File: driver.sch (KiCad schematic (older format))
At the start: 53 parts, among them J1 Screw_Terminal_01x02, J2 Conn_02x16_Odd_Even, Q1 Q_NMOS_GDSD, Q10 Q_NMOS_GDSD, Q11 Q_NMOS_GDSD, Q12 Q_NMOS_GDSD, Q13 Q_NMOS_GDSD, Q14 Q_NMOS_GDSD, Q15 Q_NMOS_GDSD, Q16 Q_NMOS_GDSD, Q17 AOD417 Q_PMOS_DGS, Q2 Q_NMOS_GDSD, Q3 Q_NMOS_GDSD, Q4 Q_NMOS_GDSD, Q5 Q_NMOS_GDSD, Q6 Q_NMOS_GDSD, Q7 Q_NMOS_GDSD, Q8 Q_NMOS_GDSD, Q9 Q_NMOS_GDSD, SW1 SW_Push, U1 PCA9685PW

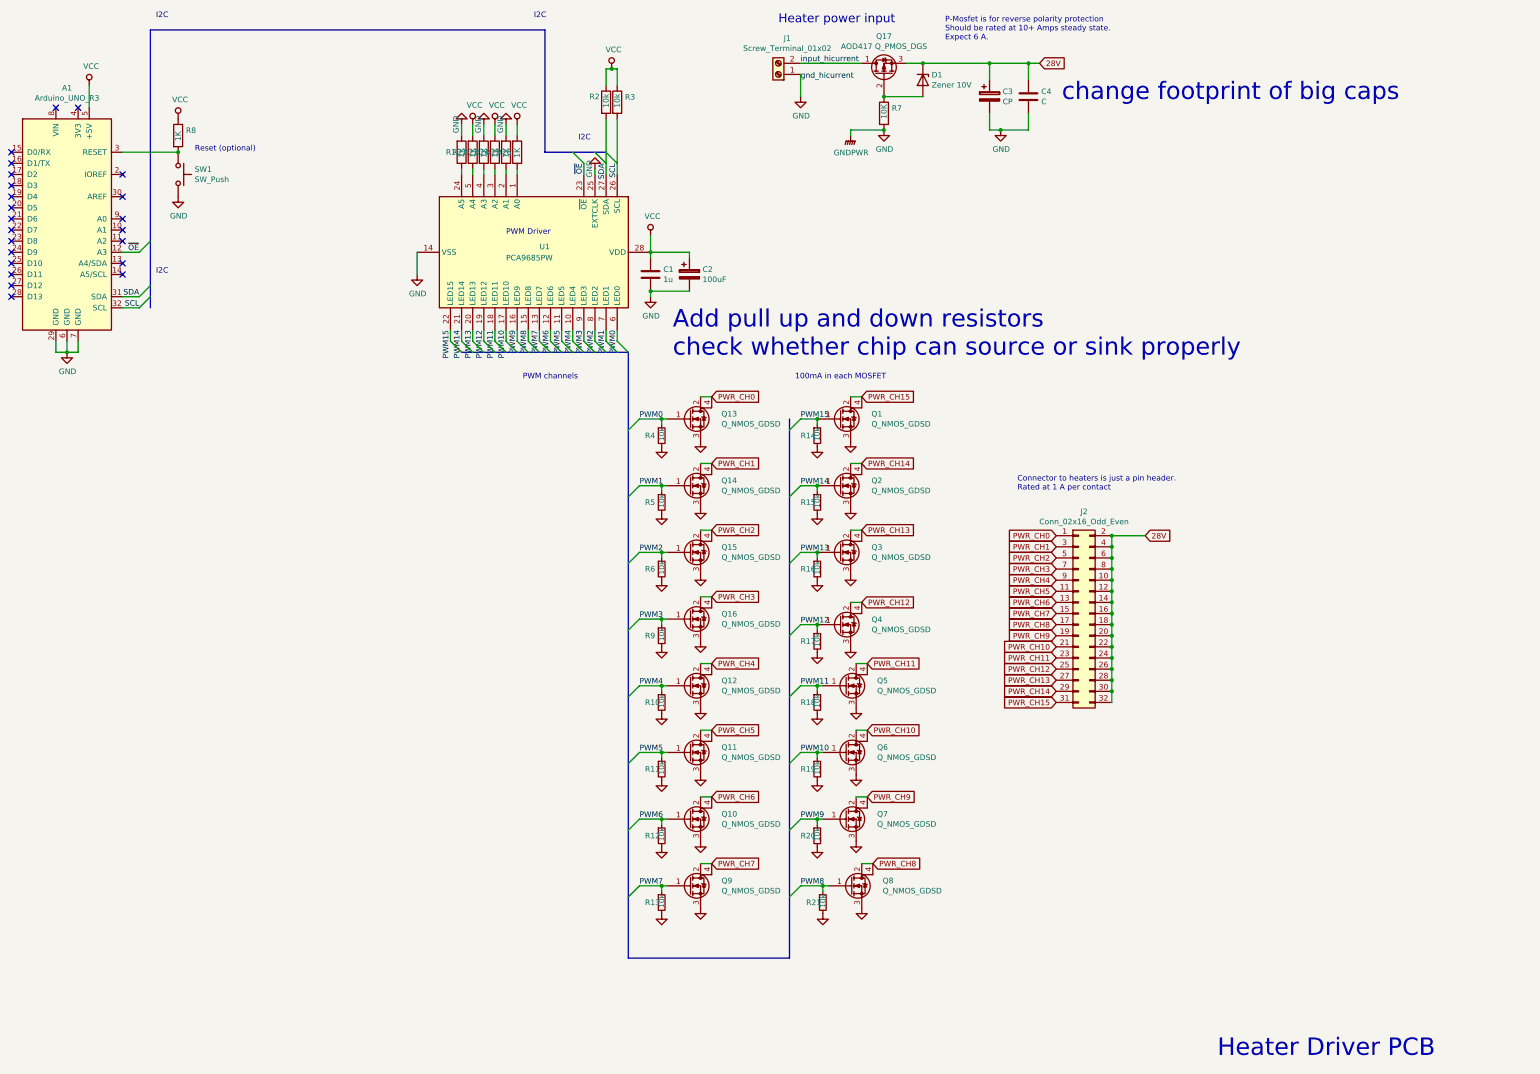
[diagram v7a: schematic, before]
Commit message: Change all resistors to 10K 0805. More routing and placement
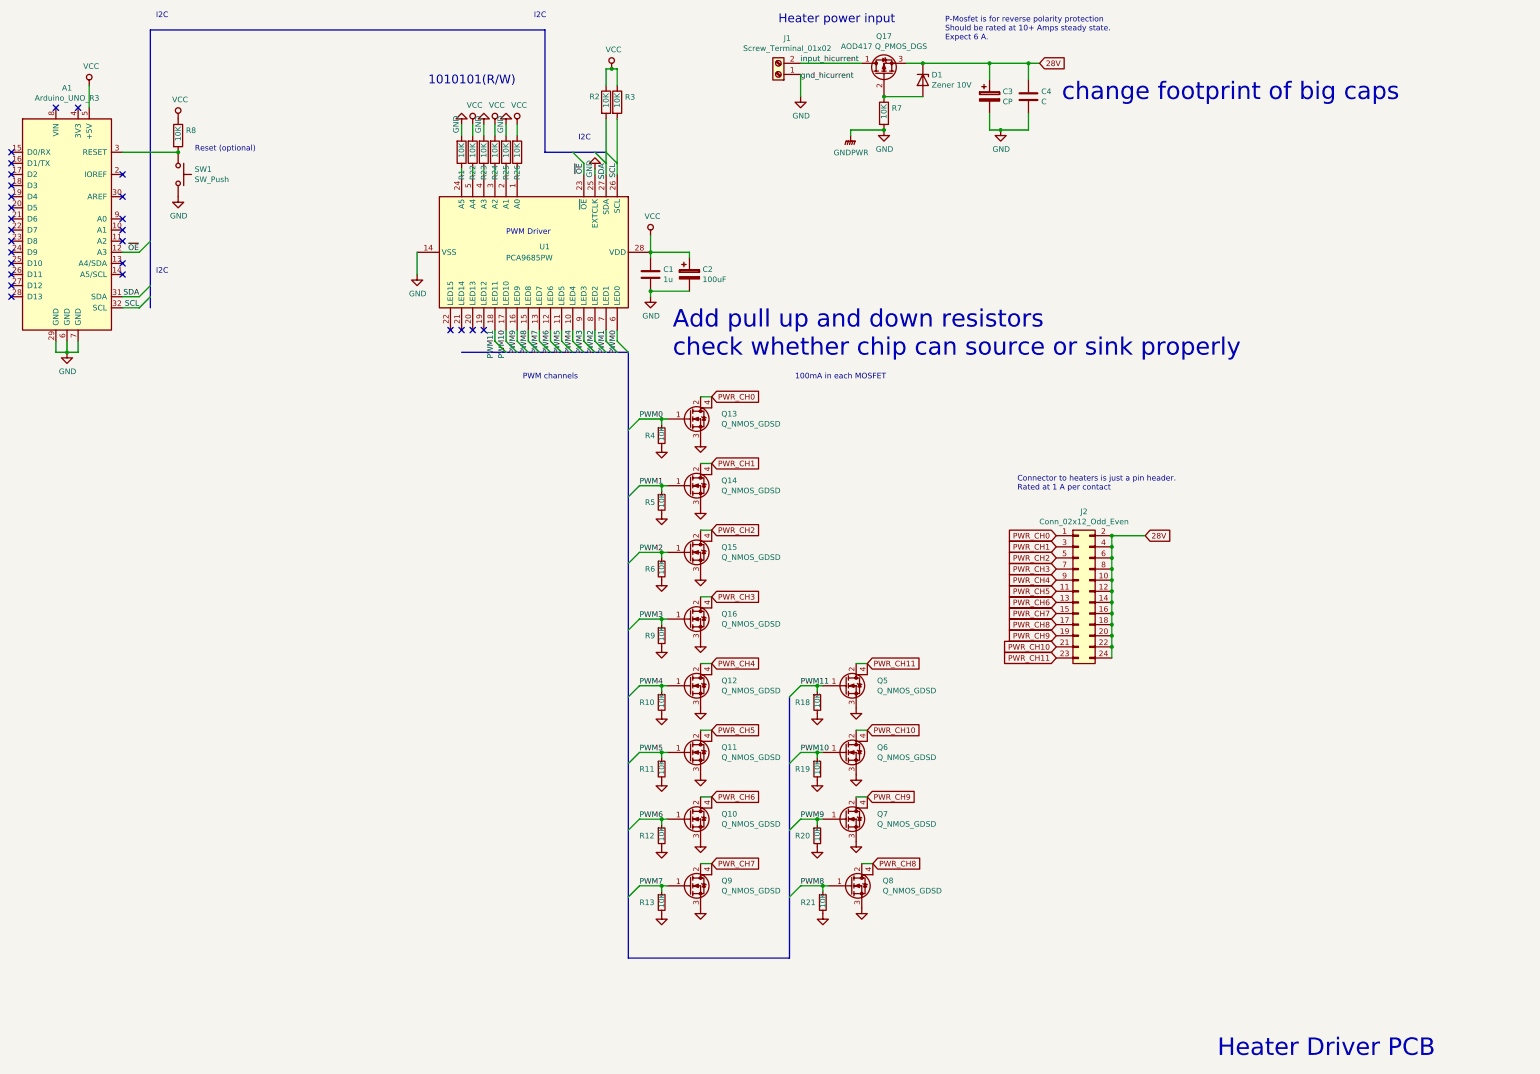
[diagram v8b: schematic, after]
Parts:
- removed J2: Conn_02x16_Odd_Even, Connector_PinHeader_2.54mm:PinHeader_2x16_P2.54mm_Vertical, symbol Connector_Generic:Conn_02x16_Odd_Even
- removed Q1, Q2, Q3, Q4: Q_NMOS_GDSD, Package_TO_SOT_SMD:SOT-223, symbol Device:Q_NMOS_GDSD
- removed R14, R15, R16, R17: 10k, Resistor_SMD:R_0805_2012Metric_Pad1.15x1.40mm_HandSolder, symbol Device:R_Small
- added J2: Conn_02x12_Odd_Even, Connector_PinHeader_2.54mm:PinHeader_2x12_P2.54mm_Vertical, symbol Connector_Generic:Conn_02x12_Odd_Even
- R1, R22, R23, R24, R25, R26, R8: value 1K -> 10K
- R10, R11, R12, R13, R18, R19, R2, R20, R21, R3, R4, R5, R6, R9: value 10k -> 10K
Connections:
- net 28V: now also J2.10 (Pin_10), J2.12 (Pin_12), J2.14 (Pin_14), J2.16 (Pin_16), J2.18 (Pin_18), J2.2 (Pin_2), J2.20 (Pin_20), J2.22 (Pin_22), J2.24 (Pin_24), J2.4 (Pin_4), J2.6 (Pin_6), J2.8 (Pin_8)
- net PWR_CH0: now also J2.1 (Pin_1)
- net PWR_CH1: now also J2.3 (Pin_3)
- net PWR_CH10: now also J2.21 (Pin_21)
- net PWR_CH11: now also J2.23 (Pin_23)
- net PWR_CH2: now also J2.5 (Pin_5)
- net PWR_CH3: now also J2.7 (Pin_7)
- net PWR_CH4: now also J2.9 (Pin_9)
- net PWR_CH5: now also J2.11 (Pin_11)
- net PWR_CH6: now also J2.13 (Pin_13)
- net PWR_CH7: now also J2.15 (Pin_15)
- net PWR_CH8: now also J2.17 (Pin_17)
- net PWR_CH9: now also J2.19 (Pin_19)
- net PWM12: no longer names the net of U1.19 (LED12)
- net PWM13: no longer names the net of U1.20 (LED13)
- net PWM14: no longer names the net of U1.21 (LED14)
- net PWM15: no longer names the net of U1.22 (LED15)
- no-connect marks 23 -> 27
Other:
- note added: "1010101(R/W)"
